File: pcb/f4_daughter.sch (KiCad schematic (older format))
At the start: 0 parts

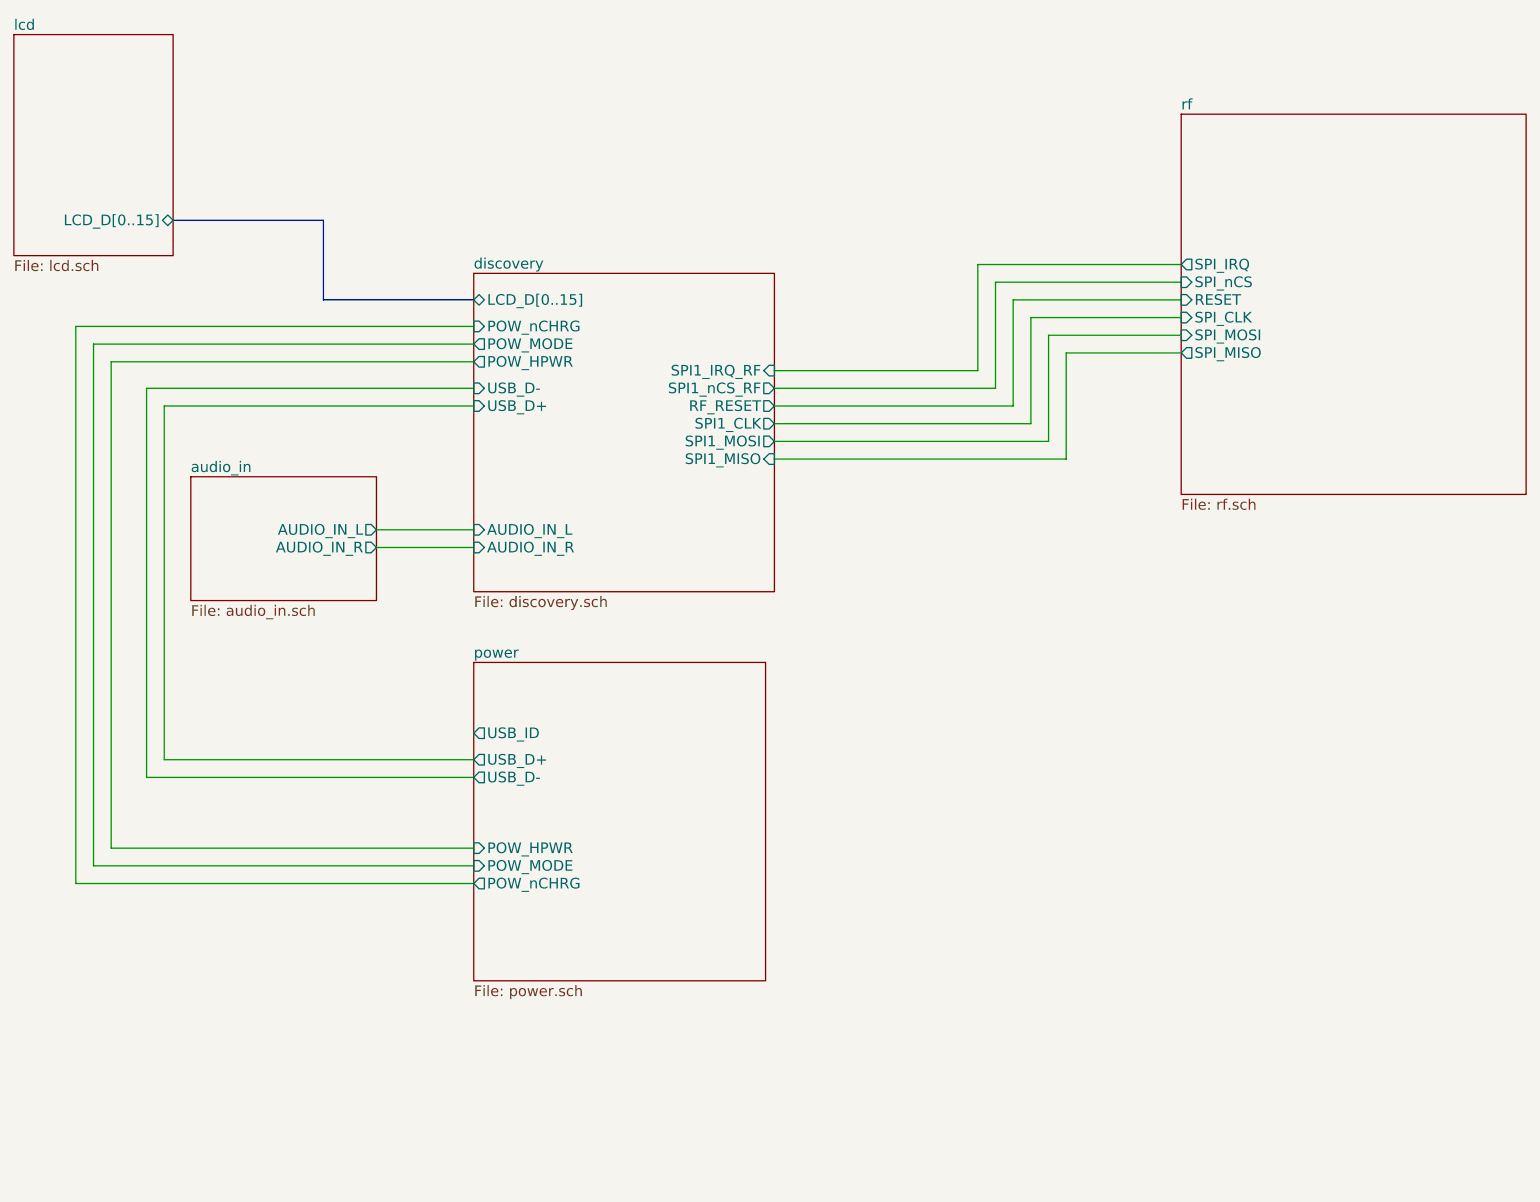
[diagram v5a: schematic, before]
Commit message: Added step-up converter in the schematics files
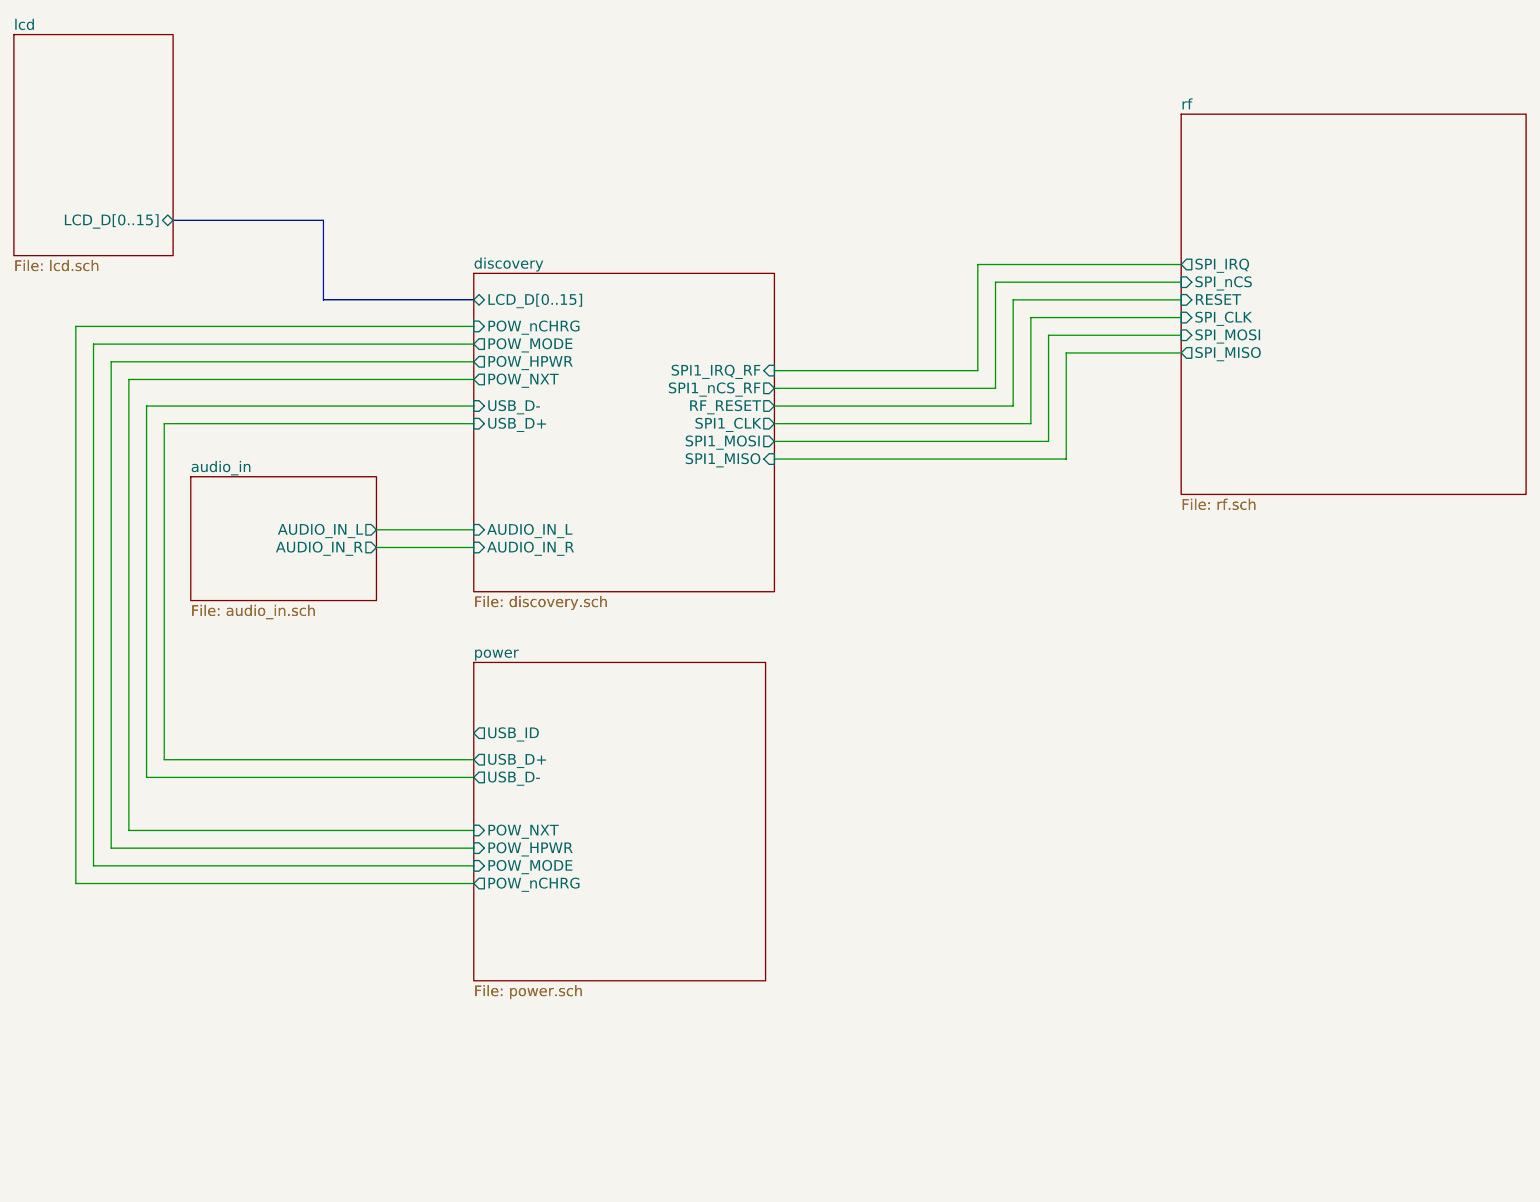
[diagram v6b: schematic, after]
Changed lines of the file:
@@
-EESchema Schematic File Version 2  date Fri 07 Sep 2012 05:49:39 PM EDT
+EESchema Schematic File Version 2  date 9/9/2012 8:55:02 PM
 LIBS:power
 LIBS:device
@@
 Sheet 1 6
 Title ""
-Date "7 sep 2012"
+Date "10 sep 2012"
 Rev ""
 Comp ""
@@
 $EndDescr
 Wire Wire Line
-	3950 5300 1900 5300
+	3950 5200 2000 5200
 Wire Wire Line
-	1900 5300 1900 2550
+	2000 5200 2000 2650
 Wire Wire Line
-	1900 2550 3950 2550
+	2000 2650 3950 2650
 Wire Wire Line
-	3950 5500 1700 5500
+	3950 5400 1800 5400
 Wire Wire Line
-	1700 5500 1700 2350
+	1800 5400 1800 2450
 Wire Wire Line
-	1700 2350 3950 2350
+	1800 2450 3950 2450
 Wire Wire Line
-	3950 2800 2200 2800
+	3950 2800 2100 2800
 Wire Wire Line
-	2200 2800 2200 4800
+	2100 2800 2100 4900
 Wire Wire Line
-	2200 4800 3950 4800
+	2100 4900 3950 4900
+Wire Wire Line
+	3950 3600 3400 3600
+Wire Bus Line
+	2250 1750 3100 1750
+Wire Bus Line
+	3100 1750 3100 2200
+Wire Bus Line
+	3100 2200 3950 2200
+Wire Wire Line
+	7950 2400 7200 2400
+Wire Wire Line
+	7200 2400 7200 3000
+Wire Wire Line
+	7200 3000 5650 3000
+Wire Wire Line
+	7950 2200 7000 2200
+Wire Wire Line
+	7000 2200 7000 2800
+Wire Wire Line
+	7000 2800 5650 2800
+Wire Wire Line
+	7950 2000 6800 2000
+Wire Wire Line
+	6800 2000 6800 2600
+Wire Wire Line
+	6800 2600 5650 2600
+Wire Wire Line
+	5650 2700 6900 2700
+Wire Wire Line
+	6900 2700 6900 2100
+Wire Wire Line
+	6900 2100 7950 2100
+Wire Wire Line
+	5650 2900 7100 2900
+Wire Wire Line
+	7100 2900 7100 2300
+Wire Wire Line
+	7100 2300 7950 2300
+Wire Wire Line
+	5650 3100 7300 3100
+Wire Wire Line
+	7300 3100 7300 2500
+Wire Wire Line
+	7300 2500 7950 2500
 Wire Wire Line
 	3400 3500 3950 3500
 Wire Wire Line
-	7950 2500 7300 2500
+	3950 4800 2200 4800
 Wire Wire Line
-	7300 2500 7300 3100
+	2200 4800 2200 2900
 Wire Wire Line
-	7300 3100 5650 3100
+	2200 2900 3950 2900
 Wire Wire Line
-	7950 2300 7100 2300
+	3950 2350 1700 2350
 Wire Wire Line
-	7100 2300 7100 2900
+	1700 2350 1700 5500
 Wire Wire Line
-	7100 2900 5650 2900
+	1700 5500 3950 5500
 Wire Wire Line
-	7950 2100 6900 2100
+	3950 2550 1900 2550
 Wire Wire Line
-	6900 2100 6900 2700
+	1900 2550 1900 5300
 Wire Wire Line
-	6900 2700 5650 2700
-Wire Wire Line
-	5650 2600 6800 2600
-Wire Wire Line
-	6800 2600 6800 2000
-Wire Wire Line
-	6800 2000 7950 2000
-Wire Wire Line
-	5650 2800 7000 2800
-Wire Wire Line
-	7000 2800 7000 2200
-Wire Wire Line
-	7000 2200 7950 2200
-Wire Wire Line
-	5650 3000 7200 3000
-Wire Wire Line
-	7200 3000 7200 2400
-Wire Wire Line
-	7200 2400 7950 2400
-Wire Bus Line
-	3950 2200 3100 2200
-Wire Bus Line
-	3100 2200 3100 1750
-Wire Bus Line
-	3100 1750 2250 1750
-Wire Wire Line
-	3950 3600 3400 3600
-Wire Wire Line
-	3950 4900 2100 4900
-Wire Wire Line
-	2100 4900 2100 2700
-Wire Wire Line
-	2100 2700 3950 2700
-Wire Wire Line
-	3950 2450 1800 2450
-Wire Wire Line
-	1800 2450 1800 5400
-Wire Wire Line
-	1800 5400 3950 5400
+	1900 5300 3950 5300
 $Sheet
 S 7950 1150 1950 2150
@@
 F0 "discovery" 60
 F1 "discovery.sch" 60
-F2 "USB_D-" I L 3950 2700 60
-F3 "USB_D+" I L 3950 2800 60
+F2 "USB_D-" I L 3950 2800 60
+F3 "USB_D+" I L 3950 2900 60
 F4 "AUDIO_IN_L" I L 3950 3500 60
 F5 "AUDIO_IN_R" I L 3950 3600 60
@@
 F14 "POW_MODE" O L 3950 2450 60
 F15 "POW_nCHRG" I L 3950 2350 60
+F16 "POW_NXT" O L 3950 2650 60
 $EndSheet
 $Sheet
@@
 F6 "POW_nCHRG" O L 3950 5500 60
 F7 "POW_HPWR" I L 3950 5300 60
+F8 "POW_NXT" I L 3950 5200 60
 $EndSheet
 $Sheet

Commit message: Added voltage switching module.
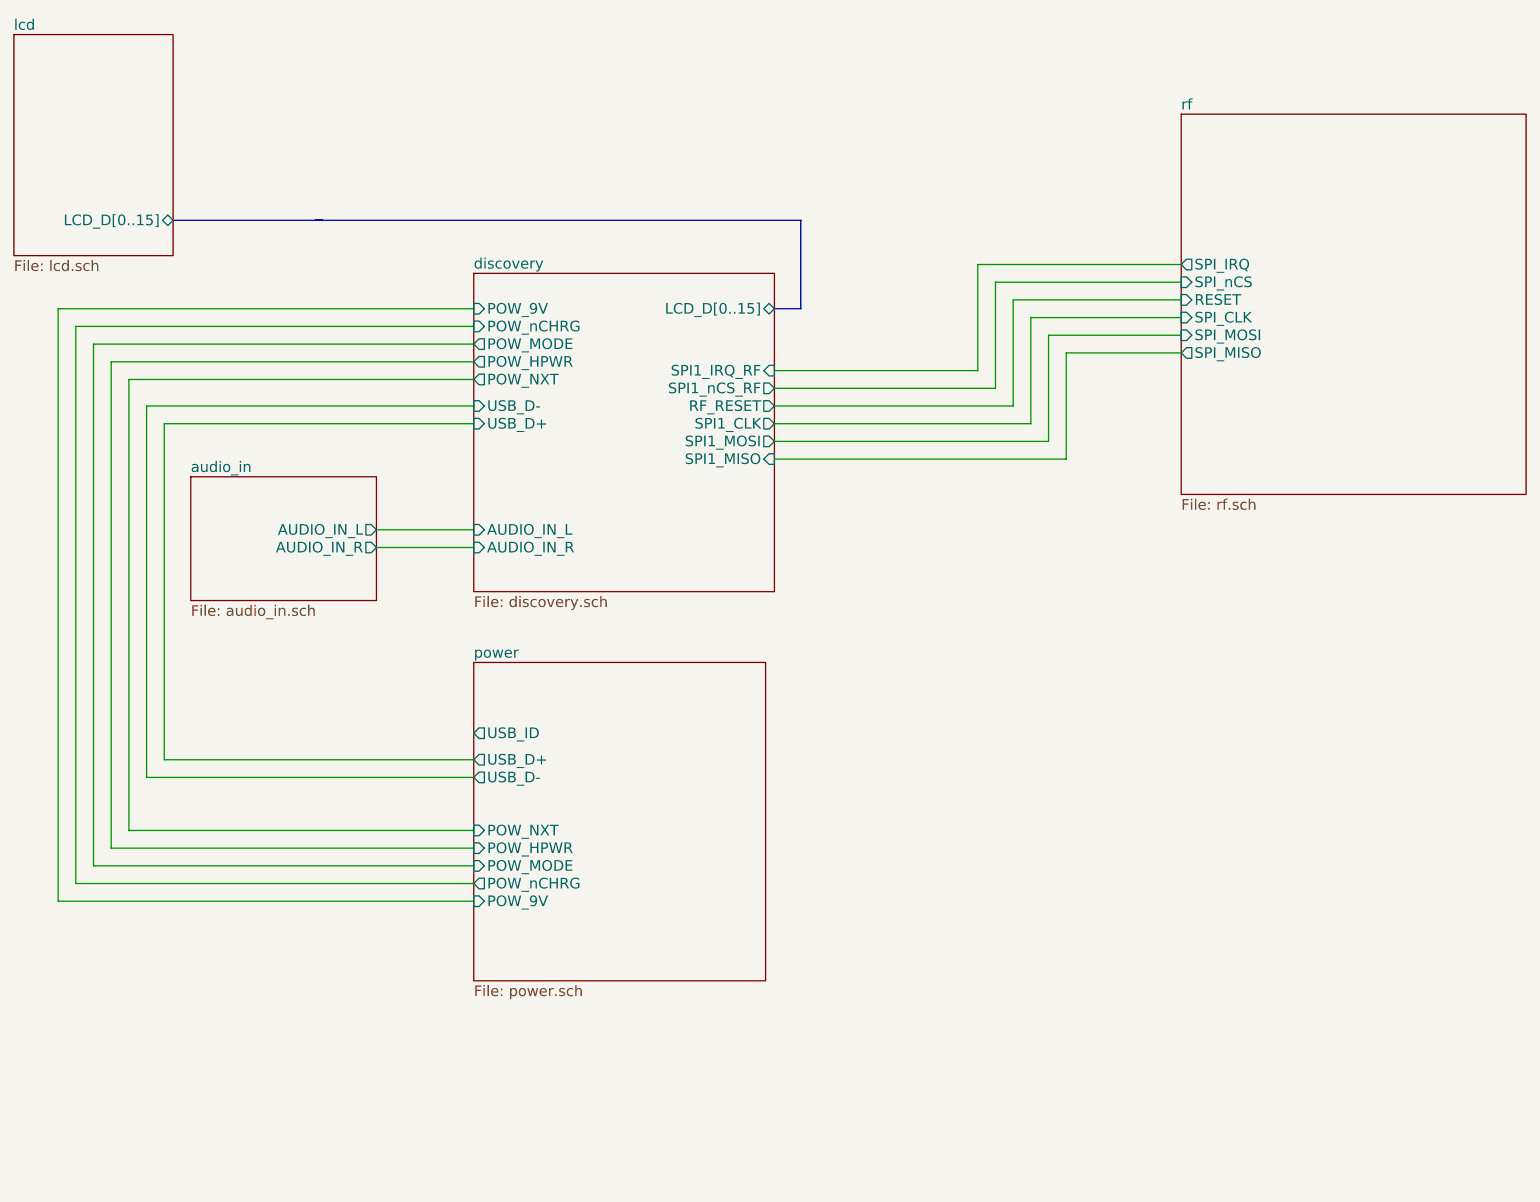
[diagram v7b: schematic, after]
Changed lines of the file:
@@
-EESchema Schematic File Version 2  date 9/9/2012 8:55:02 PM
+EESchema Schematic File Version 2  date 9/10/2012 3:24:02 PM
 LIBS:power
 LIBS:device
@@
 Comment4 ""
 $EndDescr
+Wire Bus Line
+	3050 1750 5800 1750
+Wire Bus Line
+	5800 1750 5800 2250
+Wire Bus Line
+	5800 2250 5650 2250
+Wire Wire Line
+	1600 5600 1600 2250
+Wire Wire Line
+	1600 5600 3950 5600
 Wire Wire Line
 	3950 5200 2000 5200
@@
 	3950 3600 3400 3600
 Wire Bus Line
-	2250 1750 3100 1750
-Wire Bus Line
-	3100 1750 3100 2200
-Wire Bus Line
-	3100 2200 3950 2200
+	3100 1750 2250 1750
 Wire Wire Line
 	7950 2400 7200 2400
@@
 Wire Wire Line
 	1900 5300 3950 5300
+Wire Wire Line
+	1600 2250 3950 2250
 $Sheet
 S 7950 1150 1950 2150
@@
 F4 "AUDIO_IN_L" I L 3950 3500 60
 F5 "AUDIO_IN_R" I L 3950 3600 60
-F6 "LCD_D[0..15]" B L 3950 2200 60
+F6 "LCD_D[0..15]" B R 5650 2250 60
 F7 "SPI1_IRQ_RF" I R 5650 2600 60
 F8 "SPI1_nCS_RF" O R 5650 2700 60
@@
 F15 "POW_nCHRG" I L 3950 2350 60
 F16 "POW_NXT" O L 3950 2650 60
+F17 "POW_9V" I L 3950 2250 60
 $EndSheet
 $Sheet
@@
 F7 "POW_HPWR" I L 3950 5300 60
 F8 "POW_NXT" I L 3950 5200 60
+F9 "POW_9V" I L 3950 5600 60
 $EndSheet
 $Sheet
